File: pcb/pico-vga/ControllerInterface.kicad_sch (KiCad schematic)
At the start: 63 parts

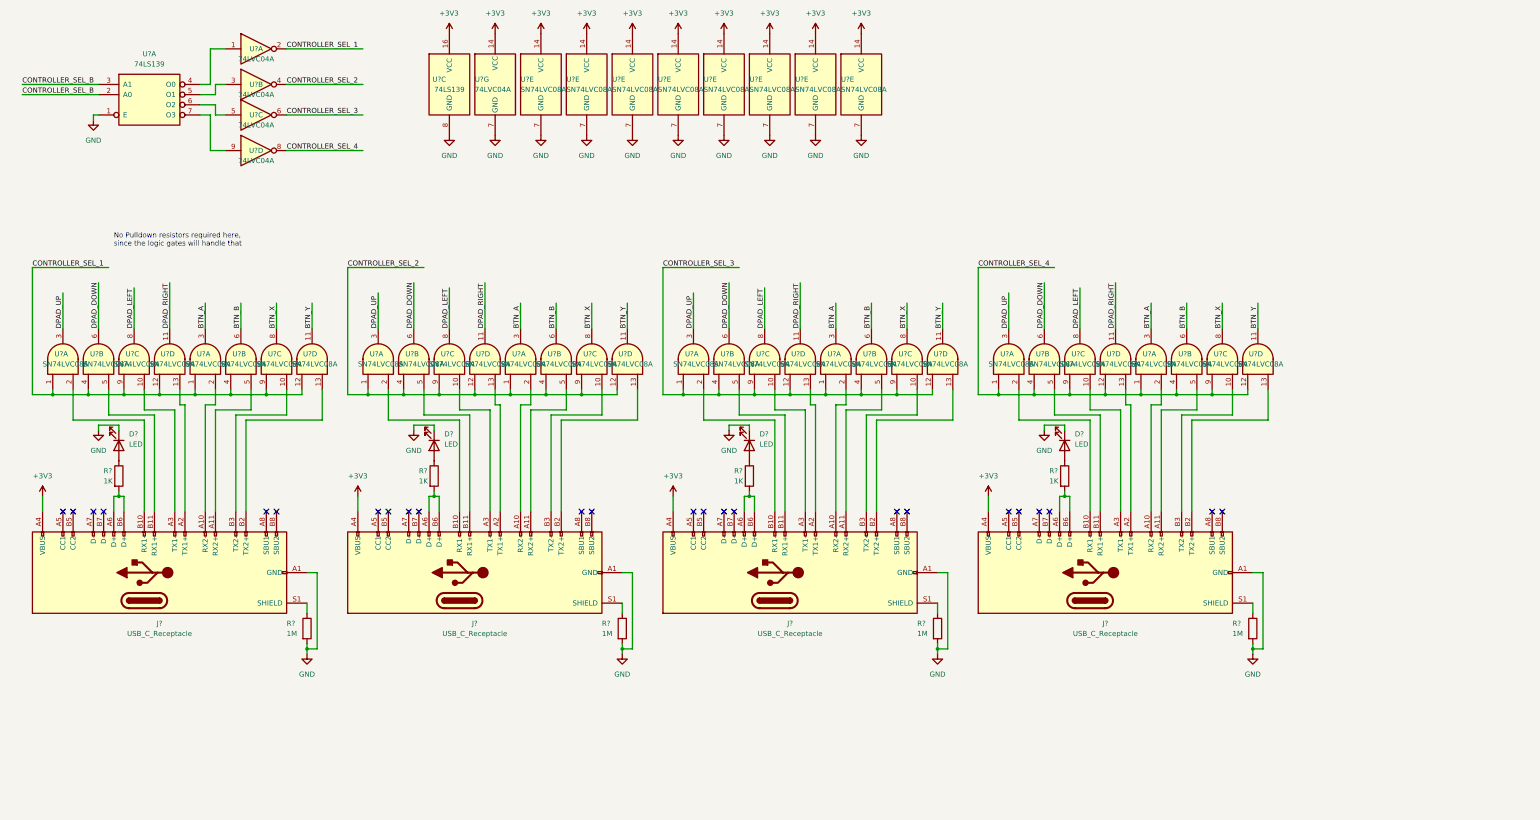
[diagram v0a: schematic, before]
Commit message: schematic completely finished, passes ERC, fully labeled
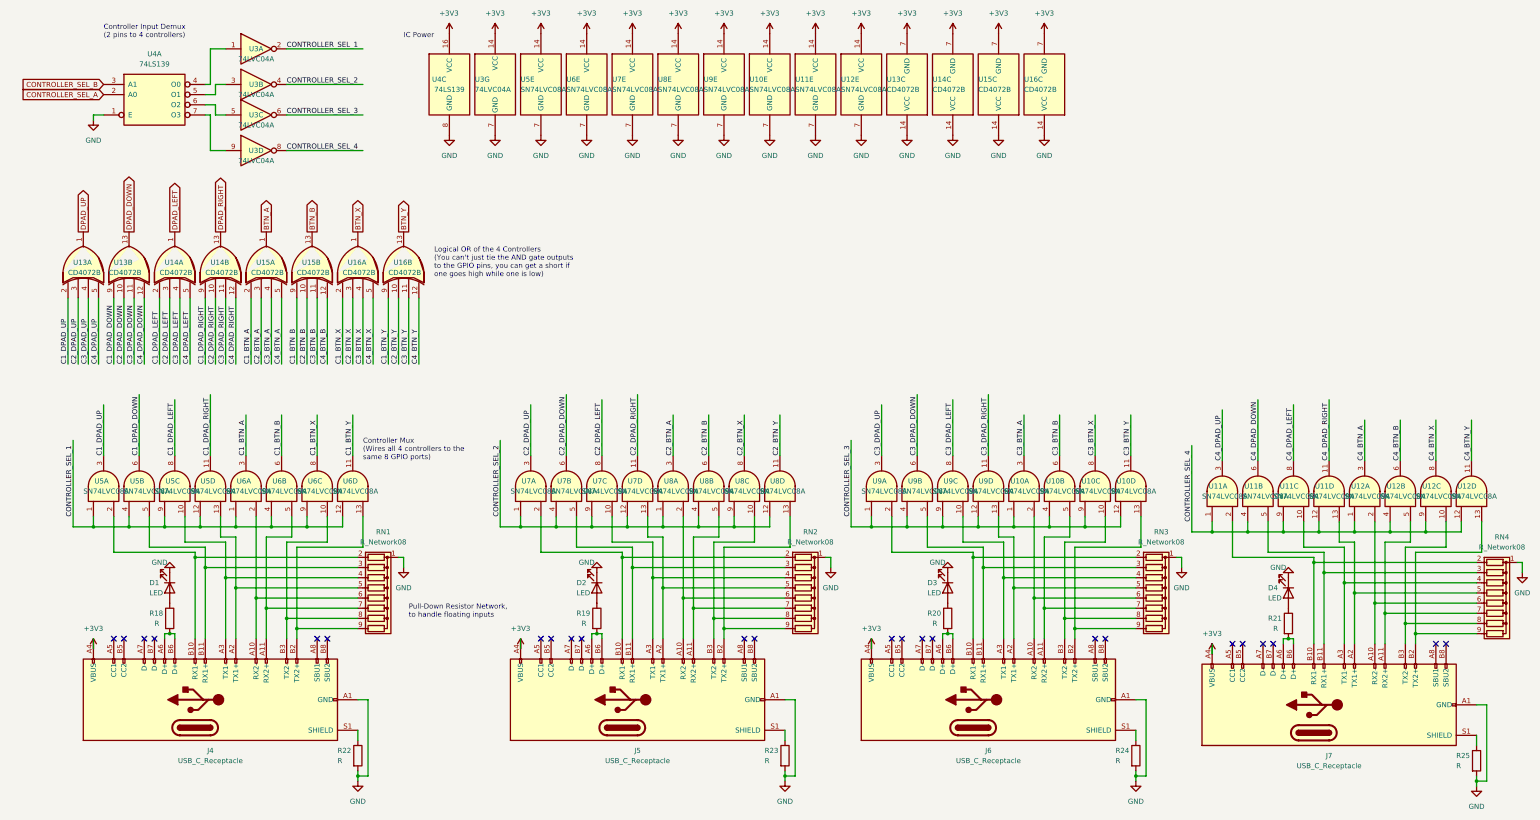
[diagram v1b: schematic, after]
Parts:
- removed D? (x3): LED, symbol Device:LED
- removed J? (x3): USB_C_Receptacle, symbol Connector:USB_C_Receptacle
- removed R? (x3): 1K, symbol Device:R
- removed R? (x3): 1M, symbol Device:R
- removed U? (x24): SN74LVC08A, symbol pico-vga:SN74LVC08A
- added D2, D3, D4: LED, symbol Device:LED
- added J5, J6, J7: USB_C_Receptacle, symbol Connector:USB_C_Receptacle
- added R19, R20, R21, R23, R24, R25: R, symbol Device:R
- added RN1, RN2, RN3, RN4: R_Network08, Resistor_THT:R_Array_SIP9, symbol Device:R_Network08
- added unit 2 of U10
- added unit 4 of U10
- added unit 1 of U10
- added unit 3 of U10
- added unit 3 of U11
- added unit 4 of U11
- added unit 1 of U11
- added unit 2 of U11
- added unit 1 of U12
- added unit 2 of U12
- added unit 3 of U12
- added unit 4 of U12
- added U13, U14, U15, U16: CD4072B, symbol pico-vga:CD4072B
- added unit 2 of U7
- added unit 4 of U7
- added unit 1 of U7
- added unit 3 of U7
- added unit 3 of U8
- added unit 2 of U8
- added unit 4 of U8
- added unit 1 of U8
- added unit 4 of U9
- added unit 3 of U9
- added unit 2 of U9
- added unit 1 of U9
- R18: renamed from R?; value 1K -> R
- R22: renamed from R?; value 1M -> R
- gave numbers to parts that had none: 12
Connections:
- net +3V3: now also J5.A4 (VBUS), J5.A9 (VBUS), J5.B4 (VBUS), J5.B9 (VBUS), J6.A4 (VBUS), J6.A9 (VBUS), J6.B4 (VBUS), J6.B9 (VBUS), J7.A4 (VBUS), J7.A9 (VBUS), J7.B4 (VBUS), J7.B9 (VBUS), U13.7 (GND), U14.7 (GND), U15.7 (GND), U16.7 (GND)
- net BTN_A: now also U15.1; no longer U6.3
- net BTN_B: now also U15.13; no longer U6.6
- net BTN_X: now also U16.1; no longer U6.8
- net BTN_Y: now also U16.13; no longer U6.11
- net CONTROLLER_SEL_2: now also U7.1, U7.12, U7.4, U7.9, U8.1, U8.12, U8.4, U8.9
- net CONTROLLER_SEL_3: now also U10.1, U10.12, U10.4, U10.9, U9.1, U9.12, U9.4, U9.9
- net CONTROLLER_SEL_4: now also U11.1, U11.12, U11.4, U11.9, U12.1, U12.12, U12.4, U12.9
- net CONTROLLER_SEL_B: no longer U4.2 (A0)
- net DPAD_DOWN: now also U13.13; no longer U5.6
- net DPAD_LEFT: now also U14.1; no longer U5.8
- net DPAD_RIGHT: now also U14.13; no longer U5.11
- net DPAD_UP: now also U13.1; no longer U5.3
- net GND: now also D2.1 (K), D3.1 (K), D4.1 (K), J5.A1 (GND), J5.A12 (GND), J5.B1 (GND), J5.B12 (GND), J6.A1 (GND), J6.A12 (GND), J6.B1 (GND), J6.B12 (GND), J7.A1 (GND), J7.A12 (GND), J7.B1 (GND), J7.B12 (GND), R23.2, R24.2, R25.2, RN1.1 (common), RN2.1 (common), RN3.1 (common), RN4.1 (common), U13.14 (VCC), U14.14 (VCC), U15.14 (VCC), U16.14 (VCC)
- net at J4.A2 (TX1+), U5.13: now also RN1.5 (R4)
- net at J4.A3 (TX1-), U5.10: now also RN1.4 (R3)
- net at J4.B3 (TX2-), U6.10: now also RN1.8 (R7)
- net at J4.B2 (TX2+), U6.13: now also RN1.9 (R8)
- net at J4.B10 (RX1-), U5.2: now also RN1.2 (R1)
- net at J4.A10 (RX2-), U6.2: now also RN1.6 (R5)
- net at J4.A11 (RX2+), U6.5: now also RN1.7 (R6)
- net at J4.B11 (RX1+), U5.5: now also RN1.3 (R2)
- new net: J5.B3 (TX2-), RN2.8 (R7), U8.10
- new net: D4.2 (A), R21.1
- new net: J7.A6 (D+), J7.B6 (D+), R21.2
- new net: J6.S1 (SHIELD), R24.1
- new net: J7.A10 (RX2-), RN4.6 (R5), U12.2
- new net: D3.2 (A), R20.1
- new net: J5.B11 (RX1+), RN2.3 (R2), U7.5
- new net: J7.A11 (RX2+), RN4.7 (R6), U12.5
- new net: J7.A2 (TX1+), RN4.5 (R4), U11.13
- new net: J7.A3 (TX1-), RN4.4 (R3), U11.10
- new net: J7.B10 (RX1-), RN4.2 (R1), U11.2
- new net: J7.B11 (RX1+), RN4.3 (R2), U11.5
- new net: J7.B2 (TX2+), RN4.9 (R8), U12.13
- new net: J7.B3 (TX2-), RN4.8 (R7), U12.10
- new net: J7.S1 (SHIELD), R25.1
- new net: J5.S1 (SHIELD), R23.1
- new net: J5.A11 (RX2+), RN2.7 (R6), U8.5
- new net: D2.2 (A), R19.1
- new net: J5.A10 (RX2-), RN2.6 (R5), U8.2
- new net: J5.A2 (TX1+), RN2.5 (R4), U7.13
- new net: J5.A3 (TX1-), RN2.4 (R3), U7.10
- new net: J5.A6 (D+), J5.B6 (D+), R19.2
- new net: J5.B10 (RX1-), RN2.2 (R1), U7.2
- new net: J5.B2 (TX2+), RN2.9 (R8), U8.13
- new net: J6.A11 (RX2+), RN3.7 (R6), U10.5
- new net: J6.B2 (TX2+), RN3.9 (R8), U10.13
- new net: J6.A2 (TX1+), RN3.5 (R4), U9.13
- new net: J6.A3 (TX1-), RN3.4 (R3), U9.10
- new net: J6.A10 (RX2-), RN3.6 (R5), U10.2
- new net: J6.B10 (RX1-), RN3.2 (R1), U9.2
- new net: J6.B11 (RX1+), RN3.3 (R2), U9.5
- new net: J6.B3 (TX2-), RN3.8 (R7), U10.10
- new net: J6.A6 (D+), J6.B6 (D+), R20.2
- new net C1_BTN_A: U15.2, U6.3
- new net C1_BTN_B: U15.9, U6.6
- new net C1_BTN_X: U16.2, U6.8
- new net C1_BTN_Y: U16.9, U6.11
- new net C1_DPAD_DOWN: U13.9, U5.6
- new net C1_DPAD_LEFT: U14.2, U5.8
- new net C1_DPAD_RIGHT: U14.9, U5.11
- new net C1_DPAD_UP: U13.2, U5.3
- new net C2_BTN_A: U15.3, U8.3
- new net C2_BTN_B: U15.10, U8.6
- new net C2_BTN_X: U16.3, U8.8
- new net C2_BTN_Y: U16.10, U8.11
- new net C2_DPAD_DOWN: U13.10, U7.6
- new net C2_DPAD_LEFT: U14.3, U7.8
- new net C2_DPAD_RIGHT: U14.10, U7.11
- new net C2_DPAD_UP: U13.3, U7.3
- new net C3_BTN_A: U10.3, U15.4
- new net C3_BTN_B: U10.6, U15.11
- new net C3_BTN_X: U10.8, U16.4
- new net C3_BTN_Y: U10.11, U16.11
- new net C3_DPAD_DOWN: U13.11, U9.6
- new net C3_DPAD_LEFT: U14.4, U9.8
- new net C3_DPAD_RIGHT: U14.11, U9.11
- new net C3_DPAD_UP: U13.4, U9.3
- new net C4_BTN_A: U12.3, U15.5
- new net C4_BTN_B: U12.6, U15.12
- new net C4_BTN_X: U12.8, U16.5
- new net C4_BTN_Y: U12.11, U16.12
- new net C4_DPAD_DOWN: U11.6, U13.12
- new net C4_DPAD_LEFT: U11.8, U14.5
- new net C4_DPAD_RIGHT: U11.11, U14.12
- new net C4_DPAD_UP: U11.3, U13.5
- new net CONTROLLER_SEL_A: U4.2 (A0)
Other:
- note added: "Controller Input Demux (2 pins to 4 controllers)"
- note added: "Controller Mux (Wires all 4 controllers to the same 8 GPIO ports)"
- note added: "IC Power"
- note added: "Logical OR of the 4 Controllers (You can't just tie the AND gate outputs to the GPIO pins, you can get a short if one goes high while one is low)"
- note added: "Pull-Down Resistor Network, to handle floating inputs"
- note removed: "No Pulldown resistors required here, since the logic gates will handle that"
- moved on the sheet: D1, J4, R18, R22, U4A, U5A, U5B, U5C, U5D, U6A, U6B, U6C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

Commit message: NOW it's complete
kicad decided to delete all of my resistor/cap values sometime before the last commit... values are back now, everything's labeled, passes ERC
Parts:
- R18, R19, R20, R21: value R -> 1K
- R22, R23, R24, R25: value R -> 1M
- RN1, RN2, RN3, RN4: value R_Network08 -> 10K
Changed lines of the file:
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@@
       (effects (font (size 1.27 1.27)) (justify left))
     )
-    (property "Value" "R" (id 1) (at 325.12 167.64 0)
+    (property "Value" "1K" (id 1) (at 325.12 167.64 0)
       (effects (font (size 1.27 1.27)) (justify left))
     )
@@
       (effects (font (size 1.27 1.27)) (justify left))
     )
-    (property "Value" "R" (id 1) (at 285.75 200.66 0)
+    (property "Value" "1M" (id 1) (at 285.75 200.66 0)
       (effects (font (size 1.27 1.27)) (justify left))
     )
@@
       (effects (font (size 1.27 1.27)) (justify left))
     )
-    (property "Value" "R" (id 1) (at 198.12 200.66 0)
+    (property "Value" "1M" (id 1) (at 198.12 200.66 0)
       (effects (font (size 1.27 1.27)) (justify left))
     )
@@
     (in_bom yes) (on_board yes)
     (property "Reference" "RN1" (id 0) (at 102.87 143.51 90))
-    (property "Value" "R_Network08" (id 1) (at 102.87 146.05 90))
+    (property "Value" "10K" (id 1) (at 102.87 146.05 90))
     (property "Footprint" "Resistor_THT:R_Array_SIP9" (id 2) (at 101.6 172.085 90)
       (effects (font (size 1.27 1.27)) hide)
@@
     (in_bom yes) (on_board yes)
     (property "Reference" "RN4" (id 0) (at 382.27 144.78 90))
-    (property "Value" "R_Network08" (id 1) (at 382.27 147.32 90))
+    (property "Value" "10K" (id 1) (at 382.27 147.32 90))
     (property "Footprint" "Resistor_THT:R_Array_SIP9" (id 2) (at 381 173.355 90)
       (effects (font (size 1.27 1.27)) hide)
@@
       (effects (font (size 1.27 1.27)) (justify left))
     )
-    (property "Value" "R" (id 1) (at 91.44 200.66 0)
+    (property "Value" "1M" (id 1) (at 91.44 200.66 0)
       (effects (font (size 1.27 1.27)) (justify left))
     )
@@
     (in_bom yes) (on_board yes)
     (property "Reference" "RN3" (id 0) (at 297.18 143.51 90))
-    (property "Value" "R_Network08" (id 1) (at 297.18 146.05 90))
+    (property "Value" "10K" (id 1) (at 297.18 146.05 90))
     (property "Footprint" "Resistor_THT:R_Array_SIP9" (id 2) (at 295.91 172.085 90)
       (effects (font (size 1.27 1.27)) hide)
@@
       (effects (font (size 1.27 1.27)) (justify left))
     )
-    (property "Value" "R" (id 1) (at 240.03 166.37 0)
+    (property "Value" "1K" (id 1) (at 240.03 166.37 0)
       (effects (font (size 1.27 1.27)) (justify left))
     )
@@
     (in_bom yes) (on_board yes)
     (property "Reference" "RN2" (id 0) (at 209.55 143.51 90))
-    (property "Value" "R_Network08" (id 1) (at 209.55 146.05 90))
+    (property "Value" "10K" (id 1) (at 209.55 146.05 90))
     (property "Footprint" "Resistor_THT:R_Array_SIP9" (id 2) (at 208.28 172.085 90)
       (effects (font (size 1.27 1.27)) hide)
@@
       (effects (font (size 1.27 1.27)) (justify left))
     )
-    (property "Value" "R" (id 1) (at 152.4 166.37 0)
+    (property "Value" "1K" (id 1) (at 152.4 166.37 0)
       (effects (font (size 1.27 1.27)) (justify left))
     )
@@
       (effects (font (size 1.27 1.27)) (justify left))
     )
-    (property "Value" "R" (id 1) (at 45.72 166.37 0)
+    (property "Value" "1K" (id 1) (at 45.72 166.37 0)
       (effects (font (size 1.27 1.27)) (justify left))
     )
@@
       (effects (font (size 1.27 1.27)) (justify left))
     )
-    (property "Value" "R" (id 1) (at 370.84 201.93 0)
-      (effects (font (size 1.27 1.27)) (justify left))
-    )
+    (property "Value" "1M" (id 1) (at 370.84 201.93 0)
+      (effects (font (size 1.27 1.27)) (justify left))
+    )

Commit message: pico-vga PCB DONE!!!!
It took many hours of work, and many headaches, but the board is finally done. It passes DRC, everything looks good.
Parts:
- removed U4: 74LS139, symbol 74xx:74LS139
- added U4: SN74LVC139A, Package_SO:SOIC-16_3.9x9.9mm_P1.27mm, symbol pico-vga:SN74LVC139A
- D2: renamed from D1; footprint (none) -> LED_SMD:LED_0805_2012Metric_Pad1.15x1.40mm_HandSolder
- D3: renamed from D2; footprint (none) -> LED_SMD:LED_0805_2012Metric_Pad1.15x1.40mm_HandSolder
- D4: renamed from D3; footprint (none) -> LED_SMD:LED_0805_2012Metric_Pad1.15x1.40mm_HandSolder
- D5: renamed from D4; footprint (none) -> LED_SMD:LED_0805_2012Metric_Pad1.15x1.40mm_HandSolder
- J4, J5, J6, J7: footprint (none) -> pico-vga:USB_C_Receptacle_Molex_2171830001
- R19: renamed from R18; footprint (none) -> Resistor_SMD:R_0603_1608Metric_Pad0.98x0.95mm_HandSolder
- R20: renamed from R19; footprint (none) -> Resistor_SMD:R_0603_1608Metric_Pad0.98x0.95mm_HandSolder
- R21: renamed from R20; footprint (none) -> Resistor_SMD:R_0603_1608Metric_Pad0.98x0.95mm_HandSolder
- R22: renamed from R21; footprint (none) -> Resistor_SMD:R_0603_1608Metric_Pad0.98x0.95mm_HandSolder
- R23: renamed from R22; footprint (none) -> Resistor_SMD:R_0603_1608Metric_Pad0.98x0.95mm_HandSolder
- R24: renamed from R23; footprint (none) -> Resistor_SMD:R_0603_1608Metric_Pad0.98x0.95mm_HandSolder
- R25: renamed from R24; footprint (none) -> Resistor_SMD:R_0603_1608Metric_Pad0.98x0.95mm_HandSolder
- R26: renamed from R25; footprint (none) -> Resistor_SMD:R_0603_1608Metric_Pad0.98x0.95mm_HandSolder
- U10, U11, U12, U13, U14, U15, U16, U3, U5, U6, U7, U8, U9: footprint (none) -> Package_SO:SOIC-14_3.9x8.7mm_P1.27mm
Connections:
- net +3V3: now also U4.16 (VCC)
- net CONTROLLER_SEL_A: now also U4.2 (A0)
- net CONTROLLER_SEL_B: now also U4.3 (A1)
- net GND: now also U4.1 (E), U4.8 (GND)
- net at U3.5: now also U4.6 (O2)
- net at U3.1: now also U4.4 (O0)
- net at U3.3: now also U4.5 (O1)
- net at U3.9: now also U4.7 (O3)
